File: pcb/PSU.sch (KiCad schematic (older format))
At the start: 20 parts, among them Q3 DMG2305UX, Q4 BCM857BS, U18 XCL206B123, U9 XCL214B333

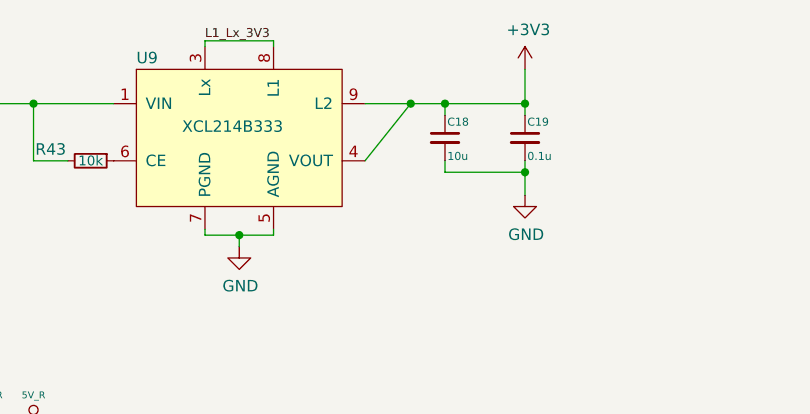
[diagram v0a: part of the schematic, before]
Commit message: Solved connections showed wrong by ERC
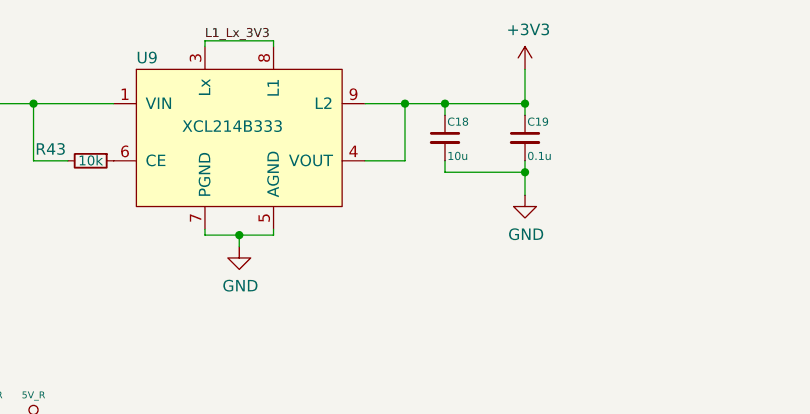
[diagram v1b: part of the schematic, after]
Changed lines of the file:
@@
 EESchema Schematic File Version 4
-LIBS:keep_breathing_ctrl-cache
 EELAYER 30 0
 EELAYER END
@@
 $EndComp
 Wire Wire Line
-	3450 1975 3650 1975
-Wire Wire Line
-	3450 2225 3650 1975
-Wire Wire Line
 	2750 1725 2750 1700
 Wire Wire Line
@@
 	1    0    0    -1
 $EndComp
-Wire Wire Line
-	3650 1975 3800 1975
-Connection ~ 3650 1975
 Connection ~ 3800 1975
 Wire Wire Line
@@
 	-1   0    0    -1
 $EndComp
+Wire Wire Line
+	3450 1975 3625 1975
+Wire Wire Line
+	3450 2225 3625 2225
+Wire Wire Line
+	3625 2225 3625 1975
+Connection ~ 3625 1975
+Wire Wire Line
+	3625 1975 3800 1975
 $EndSCHEMATC

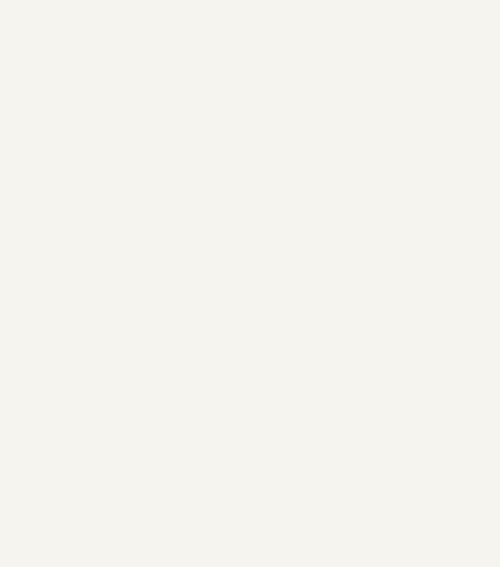
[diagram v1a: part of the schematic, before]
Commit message: Solved connection problem with XCL214B333DR and it was added 3 leds to the board
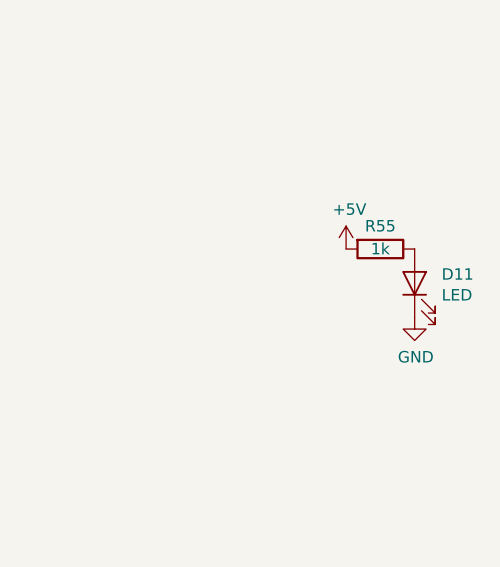
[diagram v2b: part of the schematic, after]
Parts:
- added D11: LED, LED_SMD:LED_0603_1608Metric, symbol Device:LED
- added R55: 1k, Resistor_SMD:R_0402_1005Metric, symbol Device:R
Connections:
- net +5V: now also R55.2
- net GND: now also D11.1 (K)
- new net: D11.2 (A), R55.1
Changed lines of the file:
@@
 Wire Wire Line
 	3625 1975 3800 1975
+$Comp
+L Device:R R55
+U 1 1 5EE08332
+P 9200 3900
+F 0 "R55" V 9100 3900 50  0000 C CNN
+F 1 "1k" V 9200 3900 50  0000 C CNN
+F 2 "Resistor_SMD:R_0402_1005Metric" V 9130 3900 50  0001 C CNN
+F 3 "~" H 9200 3900 50  0001 C CNN
+F 4 "" V 9200 3900 50  0001 C CNN "DigiKey"
+	1    9200 3900
+	0    1    1    0
+$EndComp
+$Comp
+L Device:LED D11
+U 1 1 5EE08E78
+P 9350 4050
+F 0 "D11" V 9389 3932 50  0000 R CNN
+F 1 "LED" V 9298 3932 50  0000 R CNN
+F 2 "LED_SMD:LED_0603_1608Metric" H 9350 4050 50  0001 C CNN
+F 3 "~" H 9350 4050 50  0001 C CNN
+F 4 "SML-D12U1WT86CT-ND" V 9350 4050 50  0001 C CNN "Field4"
+	1    9350 4050
+	0    -1   -1   0
+$EndComp
+$Comp
+L power:+5V #PWR0253
+U 1 1 5EE0A95C
+P 9050 3900
+F 0 "#PWR0253" H 9050 3750 50  0001 C CNN
+F 1 "+5V" H 9065 4073 50  0000 C CNN
+F 2 "" H 9050 3900 50  0001 C CNN
+F 3 "" H 9050 3900 50  0001 C CNN
+	1    9050 3900
+	1    0    0    -1
+$EndComp
+$Comp
+L power:GND #PWR0254
+U 1 1 5EE0B0F8
+P 9350 4200
+F 0 "#PWR0254" H 9350 3950 50  0001 C CNN
+F 1 "GND" H 9355 4027 50  0000 C CNN
+F 2 "" H 9350 4200 50  0001 C CNN
+F 3 "" H 9350 4200 50  0001 C CNN
+	1    9350 4200
+	1    0    0    -1
+$EndComp
 $EndSCHEMATC

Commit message: Added components dikey part numbers in modified sheets
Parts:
- C16: DigiKey (none) -> 478-10766-1-ND
- C17: DigiKey (none) -> 445-9066-1-ND
- C18: DigiKey (none) -> 1276-1038-1-ND
- C19, C72: DigiKey (none) -> 1276-1442-1-ND
- C20: DigiKey (none) -> 1276-1782-1-ND
- C21: DigiKey (none) -> 587-JMK107BBJ476MA-REDKR-ND
- C73: DigiKey 1276-6456-1-ND -> 1276-1044-1-ND
- C75: DigiKey 445-14751-1-ND -> 1276-1038-1-ND
- D11: DigiKey (none) -> SML-D12U1WT86CT-ND; Field4 SML-D12U1WT86CT-ND -> (none)
- D6: DigiKey (none) -> 1655-1634-1-ND
- F1: DigiKey (none) -> MF-MSMF250/16X-2CT-ND
- PWR1: DigiKey (none) -> 609-5470-ND
- Q3: DigiKey (none) -> DMG2305UX-13DICT-ND
- Q4: DigiKey (none) -> BCM857BS-7-FDIDKR-ND
- R2, R42, R43: DigiKey (none) -> 311-10KJRCT-ND
- R55: DigiKey (none) -> P1.0KJCT-ND
- R6: DigiKey (none) -> P47.0KLCT-ND
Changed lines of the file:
@@
 F 2 "SMD:PTC" H 2150 4875 60  0001 C CNN
 F 3 "" H 2150 4875 60  0001 C CNN
+F 4 "MF-MSMF250/16X-2CT-ND" H 2150 4875 50  0001 C CNN "DigiKey"
 	1    2150 4875
 	1    0    0    -1
@@
 F 2 "Package_TO_SOT_SMD:SOT-363_SC-70-6" H 2950 5450 60  0001 C CNN
 F 3 "" H 2950 5450 60  0001 C CNN
+F 4 "BCM857BS-7-FDIDKR-ND" H 2950 5450 50  0001 C CNN "DigiKey"
 	1    2950 5450
 	1    0    0    -1
@@
 F 2 "Package_TO_SOT_SMD:SOT-23" H 3150 5075 35  0001 C CNN
 F 3 "" H 2950 4975 35  0000 C CNN
+F 4 "DMG2305UX-13DICT-ND" V 2950 4975 50  0001 C CNN "DigiKey"
 	1    2950 4975
 	0    -1   -1   0
@@
 F 2 "Capacitor_SMD:C_0402_1005Metric" H 2475 5025 35  0001 C CNN
 F 3 "" H 2475 5025 35  0000 C CNN
+F 4 "445-9066-1-ND" H 2475 5025 50  0001 C CNN "DigiKey"
 	1    2475 5025
 	1    0    0    -1
@@
 F 2 "Resistor_SMD:R_0402_1005Metric" H 2800 5800 35  0001 C CNN
 F 3 "" H 2800 5800 35  0000 C CNN
+F 4 "311-10KJRCT-ND" H 2800 5800 50  0001 C CNN "DigiKey"
 	1    2800 5800
 	1    0    0    -1
@@
 F 2 "Resistor_SMD:R_0402_1005Metric" H 3100 5800 35  0001 C CNN
 F 3 "" H 3100 5800 35  0000 C CNN
+F 4 "P47.0KLCT-ND" H 3100 5800 50  0001 C CNN "DigiKey"
 	1    3100 5800
 	1    0    0    -1
@@
 F 2 "Capacitor_SMD:C_0603_1608Metric" H 1625 2225 60  0001 C CNN
 F 3 "" H 1625 2225 60  0000 C CNN
+F 4 "478-10766-1-ND" H 1625 2225 50  0001 C CNN "DigiKey"
 	1    1625 2225
 	1    0    0    -1
@@
 F 2 "SMD:DO-214AA" V 3475 5100 35  0001 C CNN
 F 3 "" V 3475 5100 35  0001 C CNN
+F 4 "1655-1634-1-ND" V 3475 5100 50  0001 C CNN "DigiKey"
 	1    3475 5100
 	0    1    1    0
@@
 F 2 "Resistor_SMD:R_0603_1608Metric" H 4650 4800 50  0001 C CNN
 F 3 "" H 4650 4800 50  0001 C CNN
+F 4 "587-JMK107BBJ476MA-REDKR-ND" H 4650 4800 50  0001 C CNN "DigiKey"
 	1    4650 4800
 	1    0    0    -1
@@
 F 2 "Resistor_SMD:R_1206_3216Metric" H 4250 4800 50  0001 C CNN
 F 3 "" H 4250 4800 50  0001 C CNN
+F 4 "1276-1782-1-ND" H 4250 4800 50  0001 C CNN "DigiKey"
 	1    4250 4800
 	1    0    0    -1
@@
 F 2 "Resistor_SMD:R_0402_1005Metric" H 5050 4800 50  0001 C CNN
 F 3 "" H 5050 4800 50  0001 C CNN
+F 4 "1276-1442-1-ND" H 5050 4800 50  0001 C CNN "DigiKey"
 	1    5050 4800
 	1    0    0    -1
@@
 F 2 "Capacitor_SMD:C_0603_1608Metric" H 8538 2250 50  0001 C CNN
 F 3 "~" H 8500 2400 50  0001 C CNN
-F 4 "445-14751-1-ND" H 8500 2400 50  0001 C CNN "DigiKey"
+F 4 "1276-1038-1-ND" H 8500 2400 50  0001 C CNN "DigiKey"
 	1    8500 2400
 	1    0    0    -1
@@
 F 2 "Capacitor_SMD:C_0603_1608Metric" H 6588 1925 50  0001 C CNN
 F 3 "~" H 6550 2075 50  0001 C CNN
-F 4 "1276-6456-1-ND" H 6550 2075 50  0001 C CNN "DigiKey"
+F 4 "1276-1044-1-ND" H 6550 2075 50  0001 C CNN "DigiKey"
 	1    6550 2075
 	1    0    0    -1
@@
 F 2 "Resistor_SMD:R_0402_1005Metric" H 7200 2050 50  0001 C CNN
 F 3 "~" H 7200 2050 50  0001 C CNN
+F 4 "311-10KJRCT-ND" V 7200 2050 50  0001 C CNN "DigiKey"
 	1    7200 2050
 	0    1    1    0
@@
 F 2 "Capacitor_SMD:C_0603_1608Metric" H 3800 2125 60  0001 C CNN
 F 3 "" H 3800 2125 60  0000 C CNN
+F 4 "1276-1038-1-ND" H 3800 2125 50  0001 C CNN "DigiKey"
 	1    3800 2125
 	1    0    0    -1
@@
 F 2 "Capacitor_SMD:C_0402_1005Metric" H 4150 2125 60  0001 C CNN
 F 3 "" H 4150 2125 60  0000 C CNN
+F 4 "1276-1442-1-ND" H 4150 2125 50  0001 C CNN "DigiKey"
 	1    4150 2125
 	1    0    0    -1
@@
 F 2 "Resistor_SMD:R_0402_1005Metric" H 2250 2225 50  0001 C CNN
 F 3 "~" H 2250 2225 50  0001 C CNN
+F 4 "311-10KJRCT-ND" V 2250 2225 50  0001 C CNN "DigiKey"
 	1    2250 2225
 	0    1    1    0
@@
 F 2 "TH:10142708-08200LF" H 1600 3675 50  0001 C CNN
 F 3 "~" H 1600 3675 50  0001 C CNN
+F 4 "609-5470-ND" H 1600 3675 50  0001 C CNN "DigiKey"
 	1    1600 3675
 	-1   0    0    1
@@
 F 2 "Resistor_SMD:R_0402_1005Metric" V 9130 3900 50  0001 C CNN
 F 3 "~" H 9200 3900 50  0001 C CNN
-F 4 "" V 9200 3900 50  0001 C CNN "DigiKey"
+F 4 "P1.0KJCT-ND" V 9200 3900 50  0001 C CNN "DigiKey"
+F 5 "" V 9200 3900 50  0001 C CNN "Field5"
 	1    9200 3900
 	0    1    1    0
@@
 F 2 "LED_SMD:LED_0603_1608Metric" H 9350 4050 50  0001 C CNN
 F 3 "~" H 9350 4050 50  0001 C CNN
-F 4 "SML-D12U1WT86CT-ND" V 9350 4050 50  0001 C CNN "Field4"
+F 4 "SML-D12U1WT86CT-ND" V 9350 4050 50  0001 C CNN "DigiKey"
 	1    9350 4050
 	0    -1   -1   0

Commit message: Added digiKey part number for some components
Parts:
- C72: DigiKey 1276-1442-1-ND -> 1276-1443-1-ND
- R2, R42, R43: DigiKey 311-10KJRCT-ND -> P10KJDKR-ND
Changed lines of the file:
@@
 F 2 "Resistor_SMD:R_0402_1005Metric" H 2800 5800 35  0001 C CNN
 F 3 "" H 2800 5800 35  0000 C CNN
-F 4 "311-10KJRCT-ND" H 2800 5800 50  0001 C CNN "DigiKey"
+F 4 "P10KJDKR-ND" H 2800 5800 50  0001 C CNN "DigiKey"
 	1    2800 5800
 	1    0    0    -1
@@
 F 2 "Resistor_SMD:R_0402_1005Metric" H 5050 4800 50  0001 C CNN
 F 3 "" H 5050 4800 50  0001 C CNN
-F 4 "1276-1442-1-ND" H 5050 4800 50  0001 C CNN "DigiKey"
+F 4 "1276-1443-1-ND" H 5050 4800 50  0001 C CNN "DigiKey"
 	1    5050 4800
 	1    0    0    -1
@@
 F 2 "Resistor_SMD:R_0402_1005Metric" H 7200 2050 50  0001 C CNN
 F 3 "~" H 7200 2050 50  0001 C CNN
-F 4 "311-10KJRCT-ND" V 7200 2050 50  0001 C CNN "DigiKey"
+F 4 "P10KJDKR-ND" V 7200 2050 50  0001 C CNN "DigiKey"
 	1    7200 2050
 	0    1    1    0
@@
 F 2 "Resistor_SMD:R_0402_1005Metric" H 2250 2225 50  0001 C CNN
 F 3 "~" H 2250 2225 50  0001 C CNN
-F 4 "311-10KJRCT-ND" V 2250 2225 50  0001 C CNN "DigiKey"
+F 4 "P10KJDKR-ND" V 2250 2225 50  0001 C CNN "DigiKey"
 	1    2250 2225
 	0    1    1    0

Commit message: Added kicad design with 4 pressure sensors for daugthers PCB Added DigiKey number for power connector
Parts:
- PWR1: DigiKey2 (none) -> 609-5464-ND; DigiKey3 (none) -> 609-5473-1-ND
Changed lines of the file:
@@
 F 3 "~" H 1600 3675 50  0001 C CNN
 F 4 "609-5470-ND" H 1600 3675 50  0001 C CNN "DigiKey"
+F 5 "609-5464-ND" H 1600 3675 50  0001 C CNN "DigiKey2"
+F 6 "609-5473-1-ND" H 1600 3675 50  0001 C CNN "DigiKey3"
 	1    1600 3675
 	-1   0    0    1
